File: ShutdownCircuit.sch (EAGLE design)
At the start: 29 parts

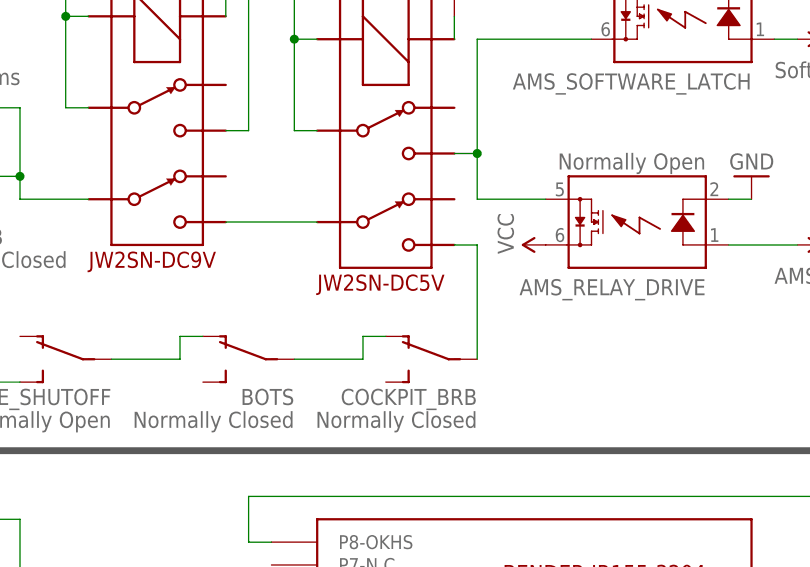
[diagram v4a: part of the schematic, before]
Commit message: Update relays in device library, update led symbol in symbol library, small fixes in external diagram, change relay in shutdown circuit
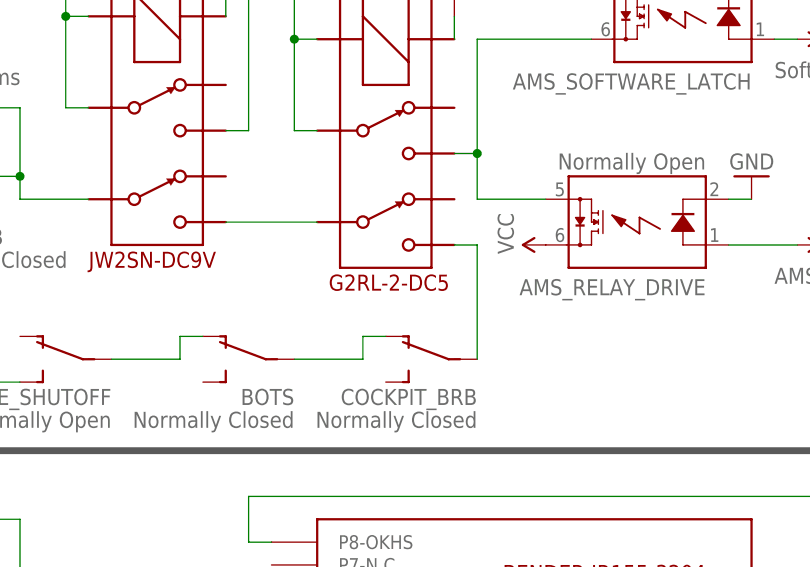
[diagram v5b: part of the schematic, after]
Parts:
- U$4: value DPDT_RELAY_PANASONIC_JW2SN-DC5V -> G2RL-2-DC5; device HyTechDevices:DPDT_RELAY_PANASONIC_JW2SN-DC5V -> HyTechDevices:G2RL-2-DC5
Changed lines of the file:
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@@
 <part name="SOFTWARE_SHUTOFF" library="HyTechSymbols" deviceset="SWITCH_SPST" device="" value="Normally Open"/>
 <part name="BSPD" library="HyTechSymbols" deviceset="SWITCH_SPST" device="" value="Normally Closed"/>
-<part name="U$4" library="HyTechDevices" deviceset="DPDT_RELAY_PANASONIC_JW2SN-DC5V" device=""/>
 <part name="GND10" library="HyTechSymbols" deviceset="GND" device=""/>
 <part name="GLV_SYSTEMS2" library="HyTechSymbols" deviceset="VIN" device="" value="VCC"/>
+<part name="U$4" library="HyTechDevices" deviceset="G2RL-2-DC5" device=""/>
 </parts>
 <sheets>
@@
 <instance part="SOFTWARE_SHUTOFF" gate="SPST" x="71.12" y="91.44" rot="MR270"/>
 <instance part="BSPD" gate="SPST" x="43.18" y="91.44" rot="MR270"/>
-<instance part="U$4" gate="-1" x="104.14" y="132.08" rot="R270"/>
 <instance part="GND10" gate="1" x="114.3" y="132.08" rot="MR180"/>
 <instance part="GLV_SYSTEMS2" gate="G$1" x="124.46" y="104.14" rot="R90"/>
+<instance part="U$4" gate="G$1" x="104.14" y="132.08" rot="R270"/>
 </instances>
 <busses>
@@
 </segment>
 <segment>
-<pinref part="U$4" gate="-1" pin="COIL+"/>
 <pinref part="GND10" gate="1" pin="GND"/>
 <wire x1="114.3" y1="129.54" x2="114.3" y2="127" width="0.1524" layer="91"/>
+<pinref part="U$4" gate="G$1" pin="COIL+"/>
 </segment>
 </net>
@@
 <wire x1="129.54" y1="127" x2="116.84" y2="127" width="0.1524" layer="91"/>
 <wire x1="116.84" y1="127" x2="116.84" y2="114.3" width="0.1524" layer="91"/>
-<pinref part="U$4" gate="-1" pin="4"/>
 <wire x1="116.84" y1="114.3" x2="114.3" y2="114.3" width="0.1524" layer="91"/>
 <pinref part="AMS_RELAY_DRIVE" gate="G$1" pin="IO2"/>
@@
 <wire x1="116.84" y1="109.22" x2="116.84" y2="114.3" width="0.1524" layer="91"/>
 <junction x="116.84" y="114.3"/>
+<pinref part="U$4" gate="G$1" pin="4"/>
 </segment>
 </net>
@@
 <net name="N$5" class="0">
 <segment>
-<pinref part="U$4" gate="-1" pin="6"/>
 <pinref part="U$1" gate="G$1" pin="5"/>
 <wire x1="88.9" y1="106.68" x2="99.06" y2="106.68" width="0.1524" layer="91"/>
+<pinref part="U$4" gate="G$1" pin="6"/>
 </segment>
 </net>
@@
 <pinref part="COCKPIT_BRB" gate="SPST" pin="P"/>
 <wire x1="116.84" y1="91.44" x2="116.84" y2="104.14" width="0.1524" layer="91"/>
-<pinref part="U$4" gate="-1" pin="5"/>
 <wire x1="116.84" y1="104.14" x2="114.3" y2="104.14" width="0.1524" layer="91"/>
+<pinref part="U$4" gate="G$1" pin="5"/>
 </segment>
 </net>
 <net name="N$16" class="0">
 <segment>
-<pinref part="U$4" gate="-1" pin="3"/>
 <wire x1="99.06" y1="116.84" x2="96.52" y2="116.84" width="0.1524" layer="91"/>
 <wire x1="96.52" y1="116.84" x2="96.52" y2="127" width="0.1524" layer="91"/>
-<pinref part="U$4" gate="-1" pin="COIL-"/>
 <wire x1="96.52" y1="127" x2="99.06" y2="127" width="0.1524" layer="91"/>
 <wire x1="96.52" y1="127" x2="96.52" y2="137.16" width="0.1524" layer="91"/>
@@
 <pinref part="AMS_SOFTWARE_LATCH" gate="G$1" pin="IO2"/>
 <wire x1="124.46" y1="132.08" x2="129.54" y2="132.08" width="0.1524" layer="91"/>
-</segment>
-</net>
+<pinref part="U$4" gate="G$1" pin="3"/>
+<pinref part="U$4" gate="G$1" pin="COIL-"/>
+</segment>
+</net>

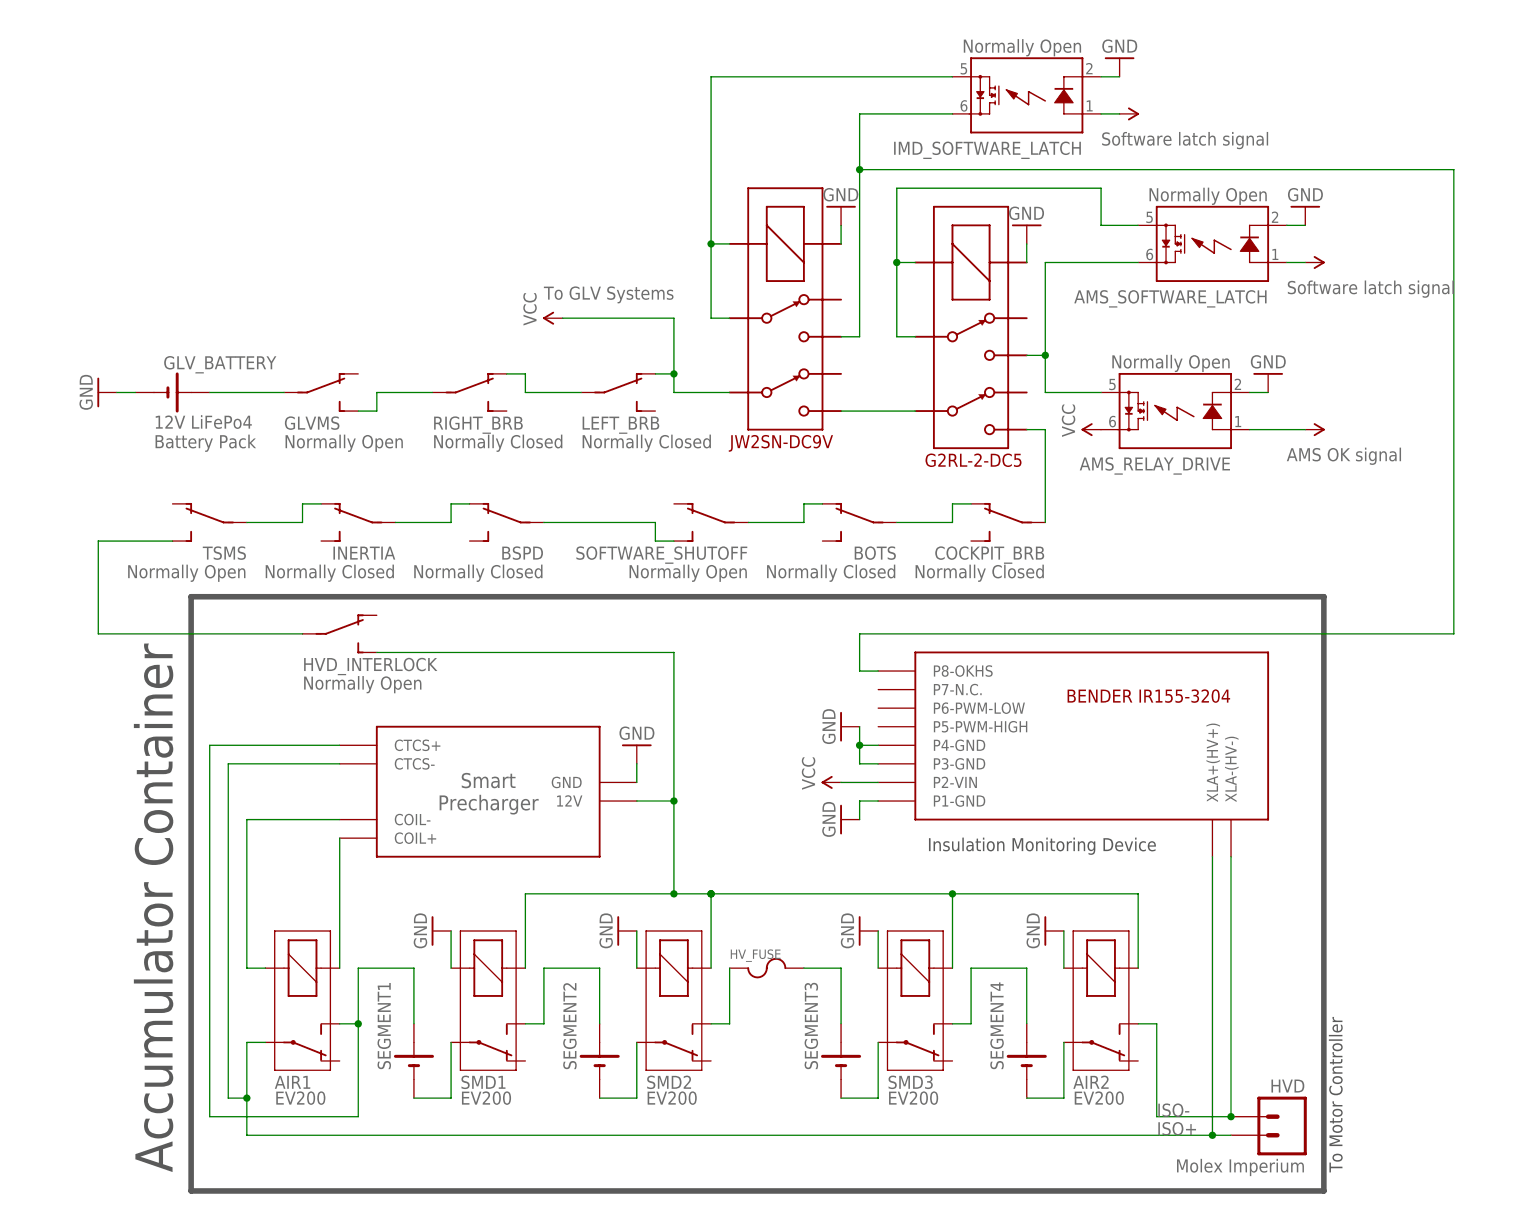
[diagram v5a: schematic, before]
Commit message: Add fuses to shutdown circuit diagram
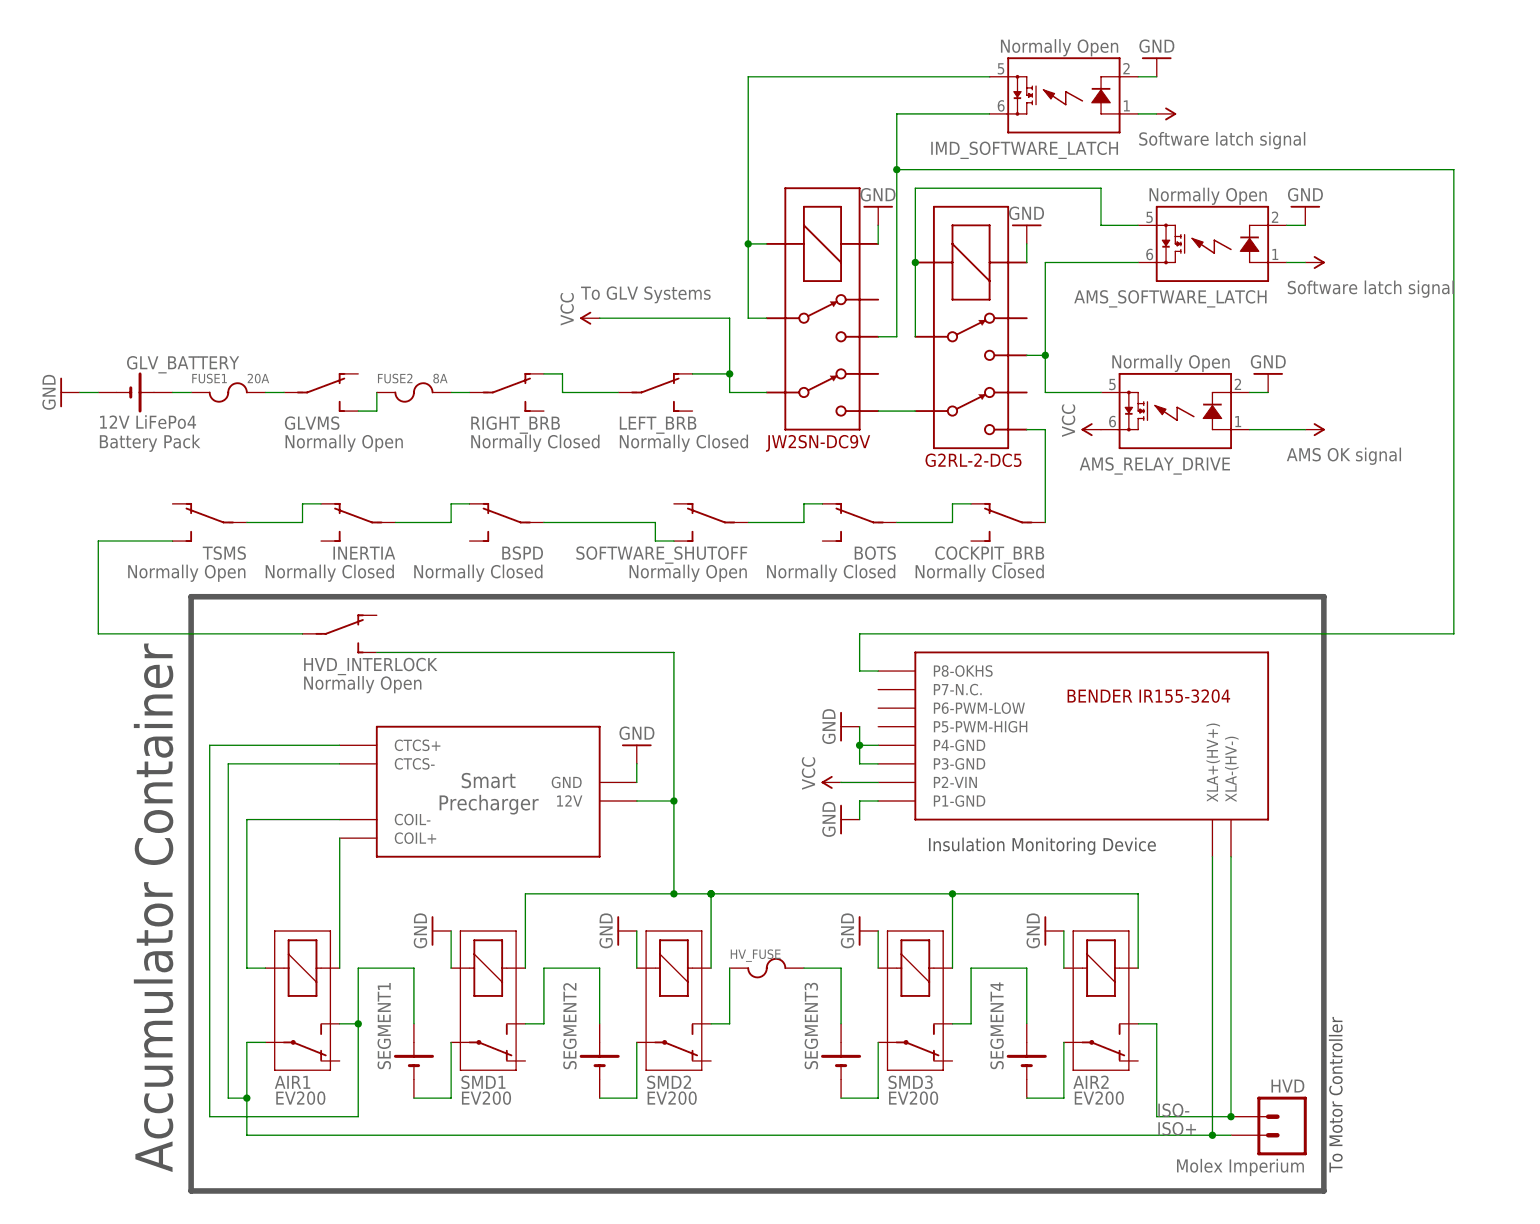
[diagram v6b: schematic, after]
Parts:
- added FUSE1: 20A, HyTechSymbols:FUSE
- added FUSE2: 8A, HyTechSymbols:FUSE
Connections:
- new net N$21: FUSE1.2, GLVMS.P
- new net N$23: FUSE2.2, RIGHT_BRB.P
- net N$1: now also FUSE1.1; no longer GLVMS.P
- net N$2: now also FUSE2.1; no longer RIGHT_BRB.P
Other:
- moved on the sheet: GLV_BATTERY, IMD_SOFTWARE_LATCH, LEFT_BRB, RIGHT_BRB

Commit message: Update shutdown circuit showing imd driver relay, change relays to omron
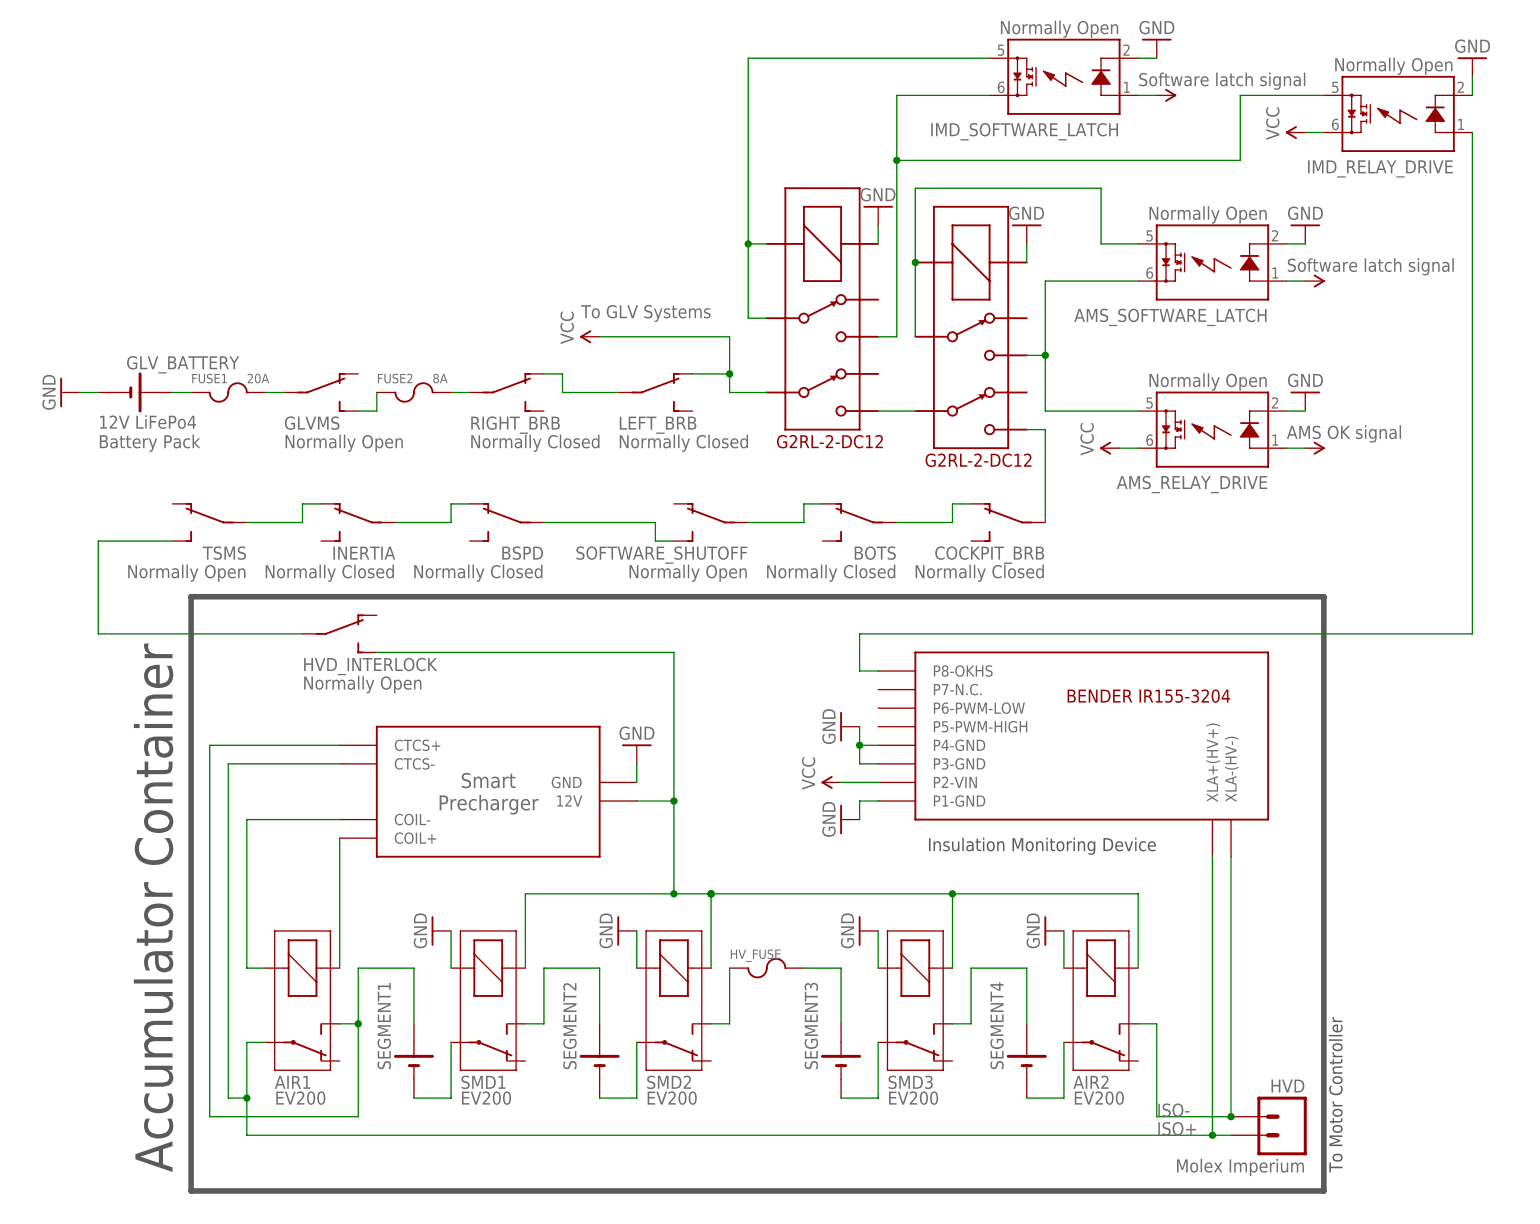
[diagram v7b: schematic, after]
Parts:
- added IMD_RELAY_DRIVE: Normally Open, HyTechDevices:SOLID_STATE_RELAY_VO14642AT
- U$1: value DPDT_RELAY_PANASONIC_JW2SN-DC9V -> G2RL-2-DC12; device HyTechDevices:DPDT_RELAY_PANASONIC_JW2SN-DC9V -> HyTechDevices:G2RL-2-DC12
- U$4: value G2RL-2-DC5 -> G2RL-2-DC12; device HyTechDevices:G2RL-2-DC5 -> HyTechDevices:G2RL-2-DC12
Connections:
- new net N$24: IMD_RELAY_DRIVE.IO2, IMD_SOFTWARE_LATCH.IO1, U$1.4
- net GND: now also IMD_RELAY_DRIVE.LED-
- net N$4: now also IMD_RELAY_DRIVE.LED+; no longer IMD_SOFTWARE_LATCH.IO1, U$1.4
- net VIN: now also IMD_RELAY_DRIVE.IO1
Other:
- moved on the sheet: AMS_RELAY_DRIVE, AMS_SOFTWARE_LATCH, IMD_SOFTWARE_LATCH
